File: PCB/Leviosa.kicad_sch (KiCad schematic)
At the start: 74 parts, among them J1 Barrel_Jack, J2 Conn_01x05_Socket, J3 2.54mm 1x03 Spare, Q1 NCE0110K, U1 STM32G030F6Px, U10 LM321, U2 TPS1H200AQDGNRQ1, U3 INA199A3DCKR, U4 L78L10_SOT89, U5 AZ1117CH2-3.3, U6 SS495A, U8 LM393, U9 MX27517

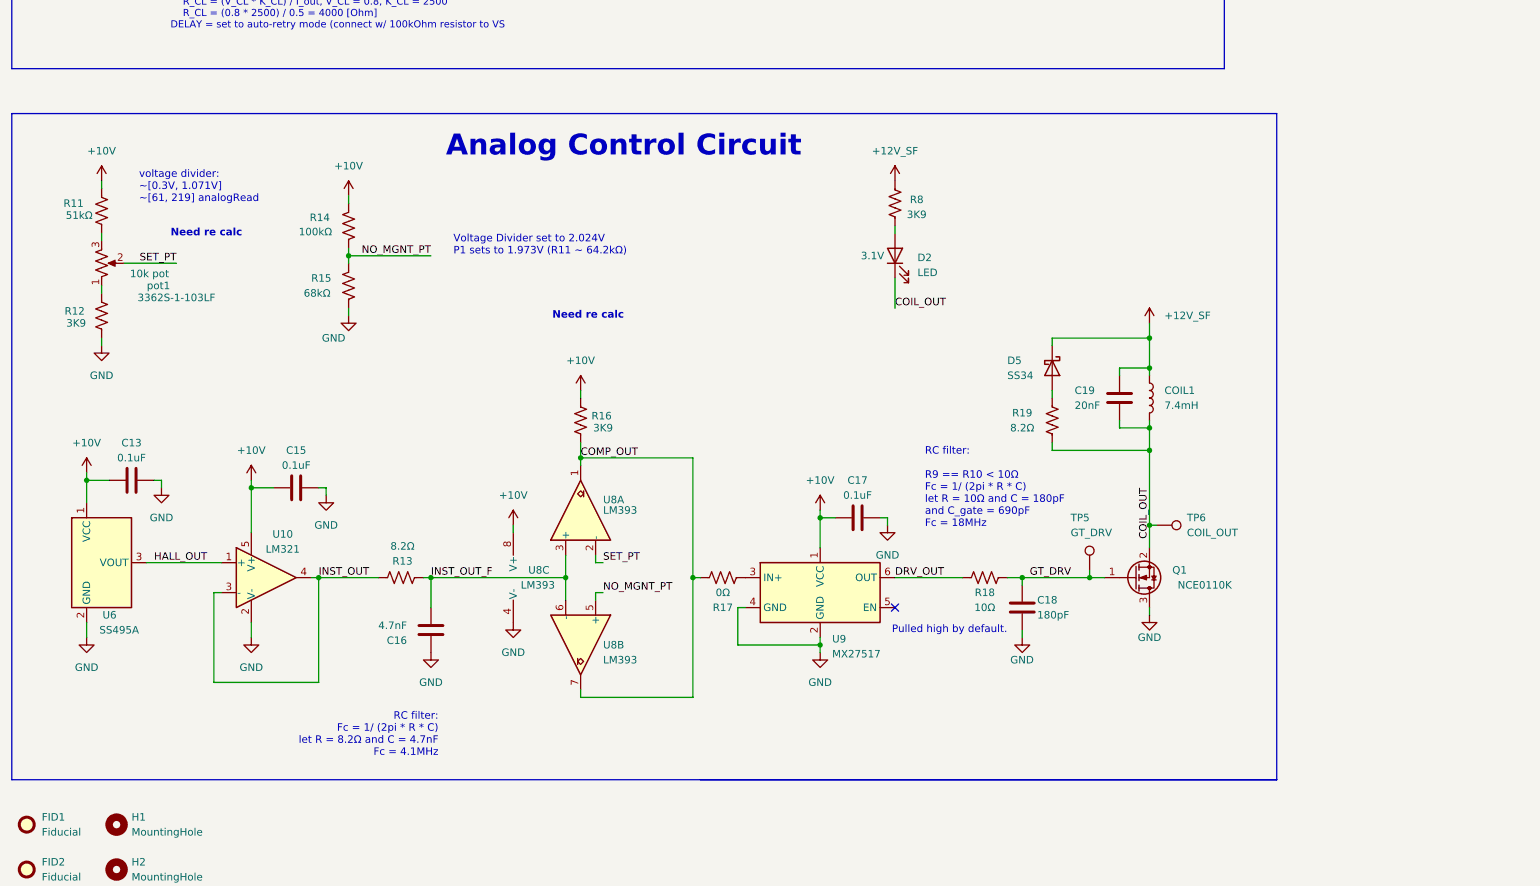
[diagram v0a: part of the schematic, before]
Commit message: Added snubber and duplicated filter to reduce part count
- Added snubber to coil output
- Changed filter from output gate driver to also be 4.1Mhz to reduce components used
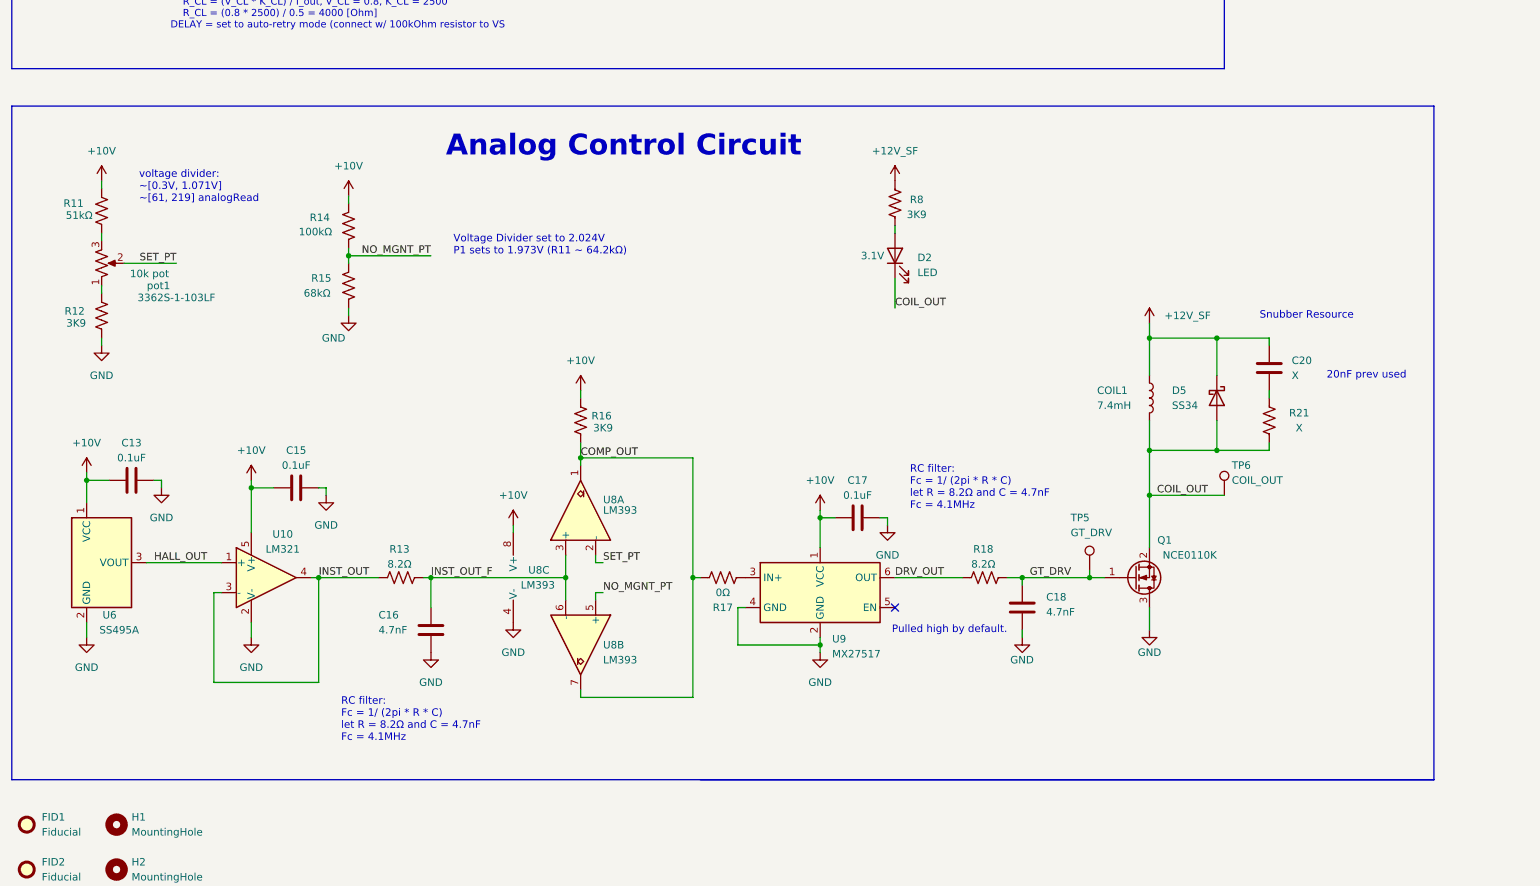
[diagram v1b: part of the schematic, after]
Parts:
- removed C19: 20nF, Capacitor_SMD:C_0805_2012Metric_Pad1.18x1.45mm_HandSolder, symbol Device:C
- removed R19: 8.2Ω, Resistor_SMD:R_1206_3216Metric, symbol Device:R_US
- added C20: X, Capacitor_SMD:C_0805_2012Metric_Pad1.18x1.45mm_HandSolder, symbol Device:C
- added R21: X, Resistor_SMD:R_0805_2012Metric_Pad1.20x1.40mm_HandSolder, symbol Device:R_US
- C18: value 180pF -> 4.7nF; footprint Capacitor_SMD:C_1206_3216Metric -> Capacitor_SMD:C_0805_2012Metric_Pad1.18x1.45mm_HandSolder; Link https://jlcpcb.com/partdetail/97327-CL31A476MPHNNNE/C96123 -> https://jlcpcb.com/partdetail/1890-0402B472K500NT/C1538
- R18: value 10Ω -> 8.2Ω; footprint Resistor_SMD:R_0603_1608Metric -> Resistor_SMD:R_1206_3216Metric
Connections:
- net +12V_SF: now also C20.1
- net COIL_OUT: now also D5.2 (A), R21.1
- net GND: now also C18.2; no longer C18.1
- net GT_DRV: now also C18.1; no longer C18.2
- new net: C20.2, R21.2
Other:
- note added: "20nF prev used"
- note added: "Snubber Resource"
- note removed: "Need re calc"
- note removed: "RC filter: R9 == R10 < 10Ω Fc = 1/ (2pi * R * C) let R = 10Ω and C = 180pF and C_gate = 690pF Fc = 18MHz"
- moved on the sheet: D5, TP6

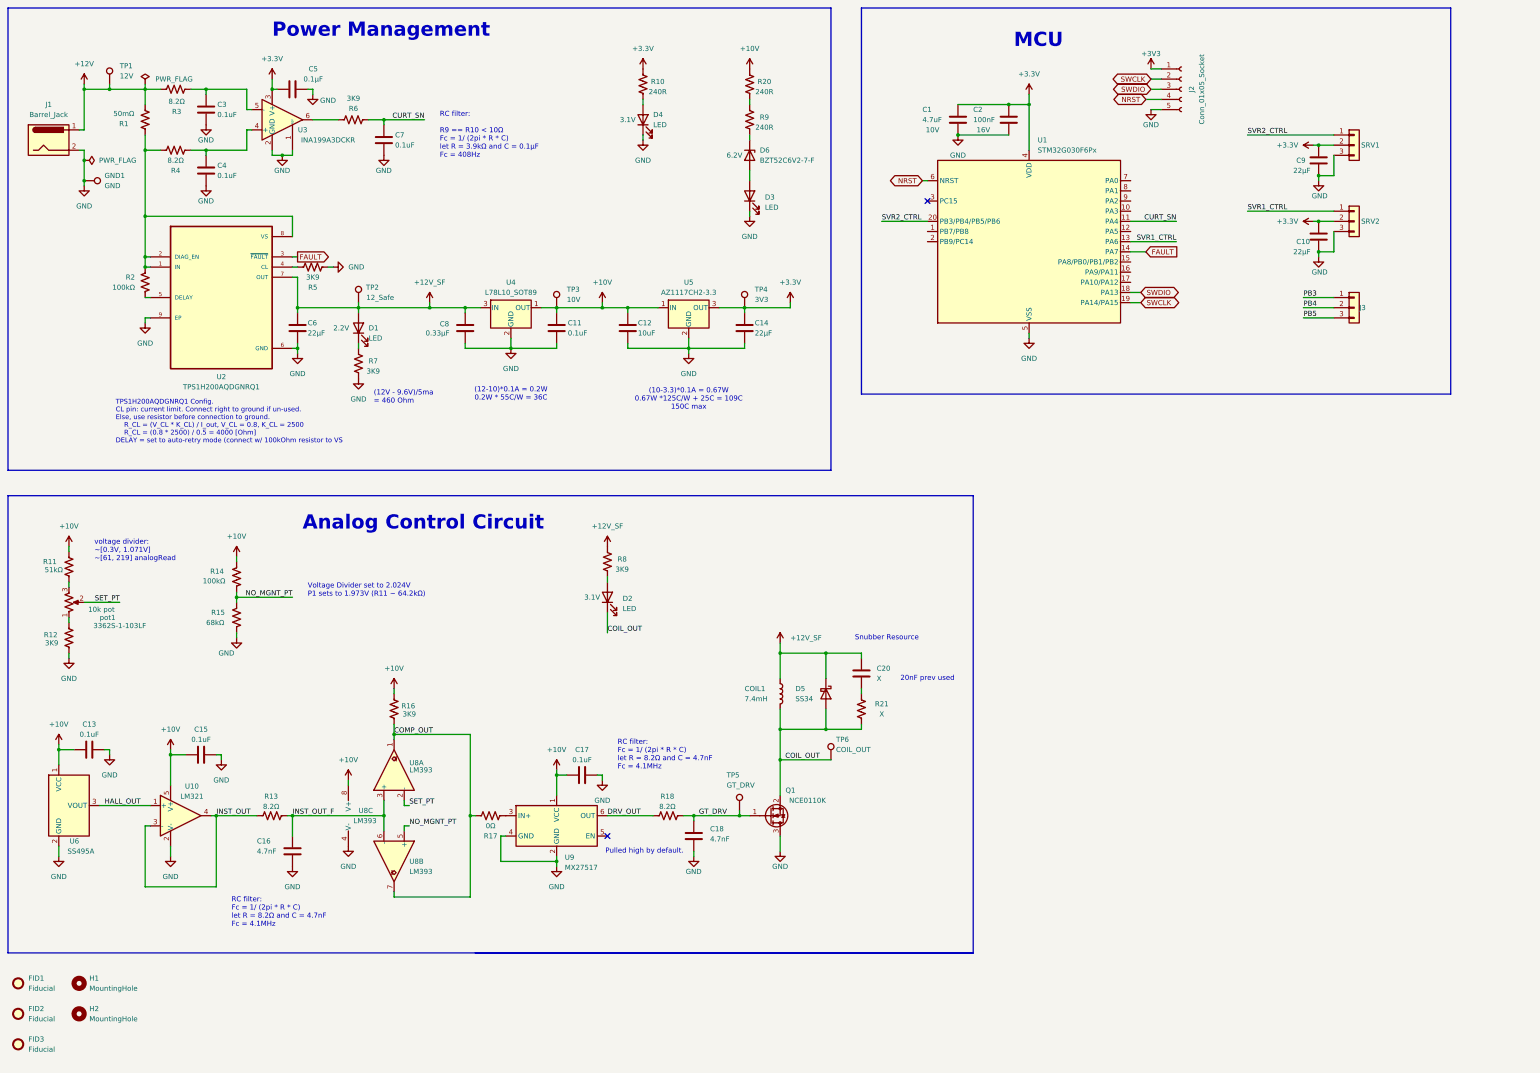
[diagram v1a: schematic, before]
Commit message: Added NC to STM32 and ran ERC
- Added power flag to VS of TPS and changed 3v3 symbol that was incorrect

- Added  blink led to STM32

- reannotated
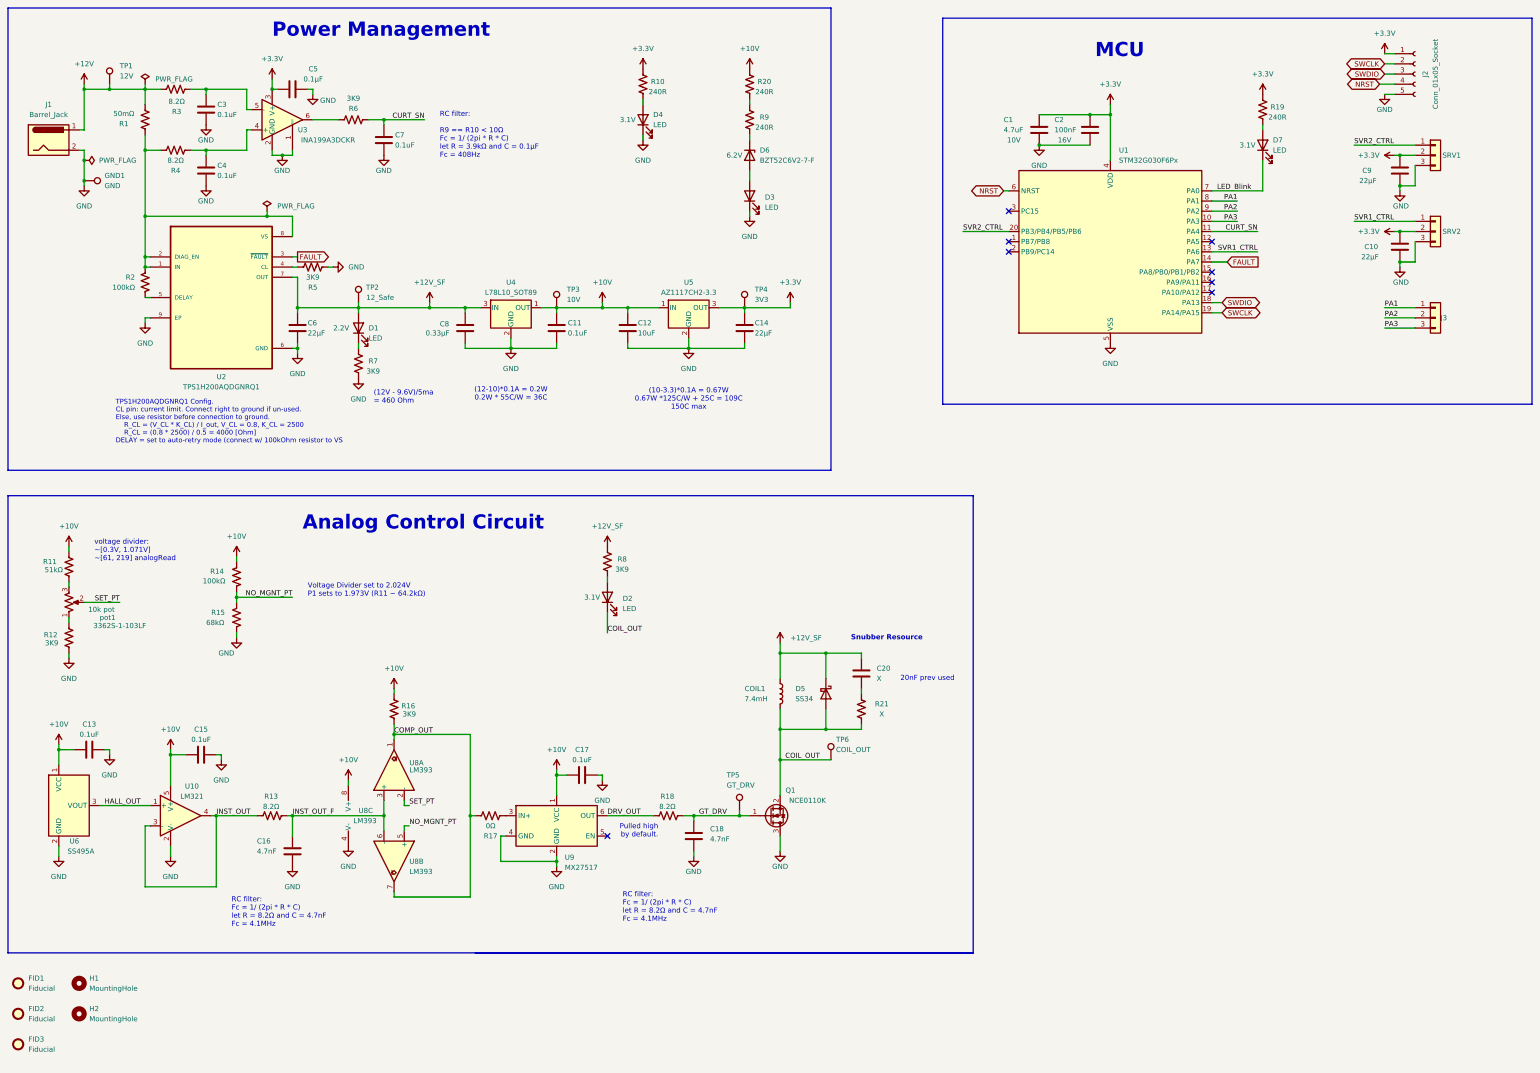
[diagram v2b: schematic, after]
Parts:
- added D7: LED, LED_SMD:LED_0603_1608Metric, symbol Device:LED
- added R19: 240R, Resistor_SMD:R_0603_1608Metric, symbol Device:R_US
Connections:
- net +3V3 is gone; now on net +3.3V: J2.1 (Pin_1)
- net PB3 is gone; now on net PA1: J3.1 (Pin_1)
- net PB4 is gone; now on net PA2: J3.2 (Pin_2)
- net PB5 is gone; now on net PA3: J3.3 (Pin_3)
- net +3.3V: now also R19.1
- net PA3: now reaches U1.10 (PA3)
- net LED_Blink: now reaches U1.7 (PA0)
- net LED_Blink: now also D7.1 (K)
- net PA1: now reaches U1.8 (PA1)
- net PA2: now reaches U1.9 (PA2)
- new net: D7.2 (A), R19.2
- no-connect marks 2 -> 8
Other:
- moved on the sheet: C1, C10, C2, C9, J2, J3, SRV1, SRV2, U1

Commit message: Update Leviosa.kicad_sch
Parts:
- renumbered C13 to C1, C11 to C10, C17 to C11, C18 to C13, C20 to C15, C1 to C16, C2 to C17, C9 to C18, C10 to C19, C15 to C2, C16 to C6, C6 to C7, C7 to C8, C8 to C9, D4 to D3, D6 to D4, D3 to D5, D5 to D6, R11 to R1, R5 to R10, R6 to R11, R7 to R12, R16 to R13, R17 to R14, R8 to R15, R10 to R16, R18 to R17, R20 to R18, R9 to R19, R12 to R2, R21 to R20, R19 to R21, R1 to R3, R2 to R4, R3 to R5, R4 to R6, R14 to R7, R15 to R8, R13 to R9, TP5 to TP4, TP4 to TP5, U6 to U1, U10 to U2, U2 to U3, U3 to U4, U8 to U5, U4 to U6, U9 to U7, U5 to U8, U1 to U9
